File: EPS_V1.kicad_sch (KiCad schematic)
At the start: 0 parts

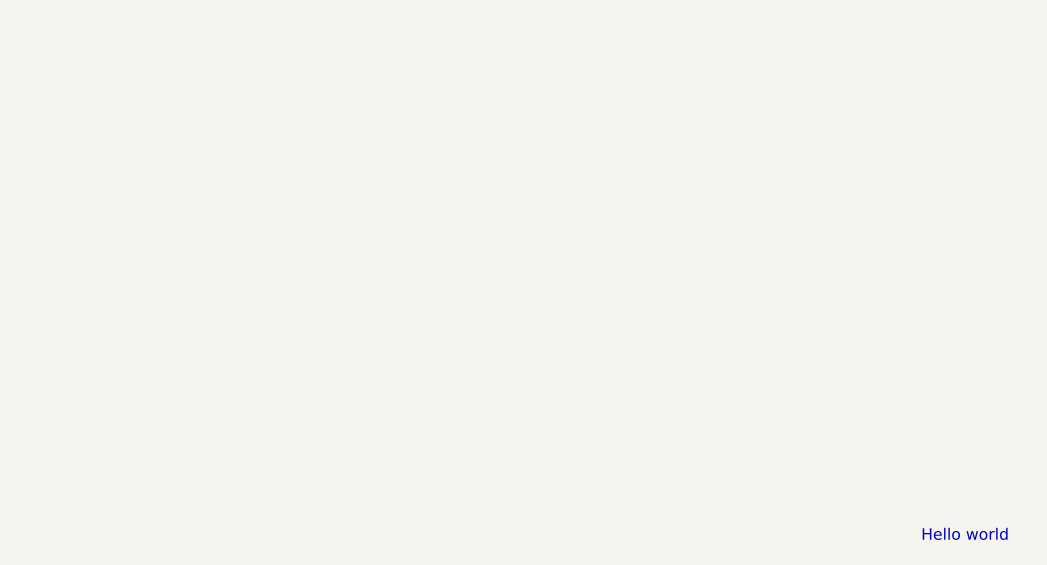
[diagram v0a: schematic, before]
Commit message: Add connectors, 5V & 3V3 buck converters, 1 battery pack & charger
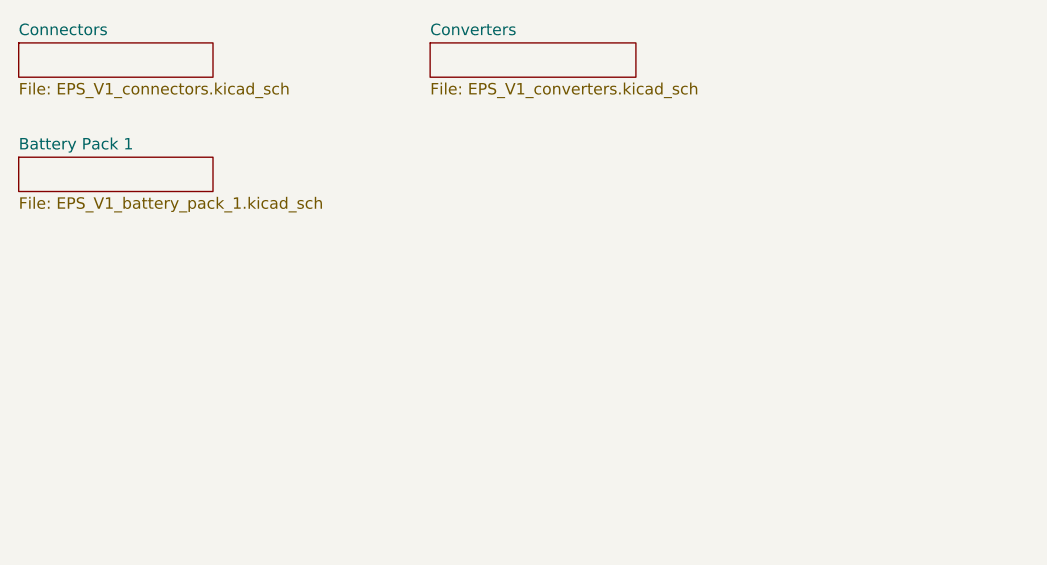
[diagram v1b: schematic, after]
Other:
- added sheet Battery Pack 1 (EPS_V1_battery_pack_1.kicad_sch)
- added sheet Connectors (EPS_V1_connectors.kicad_sch)
- added sheet Converters (EPS_V1_converters.kicad_sch)
- note removed: "Hello world"
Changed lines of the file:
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@@
 	(generator_version "9.0")
 	(paper "A4")
-	(text "Hello world"
+	(sheet
+		(at 80.01 31.75)
+		(size 22.86 3.81)
 		(exclude_from_sim no)
-		(at 139.446 86.614 0)
-		(effects
-			(font
-				(size 1.27 1.27)
+		(in_bom yes)
+		(on_board yes)
+		(dnp no)
+		(fields_autoplaced yes)
+		(stroke
+			(width 0.1524)
+			(type solid)
+		)
+		(fill
+			(color 0 0 0 0.0000)
+		)
+		(property "Sheetname" "Converters"
+			(at 80.01 31.0384 0)
+			(effects
+				(font
+					(size 1.27 1.27)
+				)
+				(justify left bottom)
 			)
 		)
+		(property "Sheetfile" "EPS_V1_converters.kicad_sch"
+			(at 80.01 36.1446 0)
+			(effects
+				(font
+					(size 1.27 1.27)
+				)
+				(justify left top)
+			)
+		)
+		(instances
+			(project "EPS_V1"
+				(path "/85157432-5d03-48fa-ab40-27ed3d133f47"
+					(page "3")
+				)
+			)
+		)
+	)
+	(sheet
+		(at 34.29 44.45)
+		(size 21.59 3.81)
+		(exclude_from_sim no)
+		(in_bom yes)
+		(on_board yes)
+		(dnp no)
+		(fields_autoplaced yes)
+		(stroke
+			(width 0.1524)
+			(type solid)
+		)
+		(fill
+			(color 0 0 0 0.0000)
+		)
+		(property "Sheetname" "Battery Pack 1"
+			(at 34.29 43.7384 0)
+			(effects
+				(font
+					(size 1.27 1.27)
+				)
+				(justify left bottom)
+			)
+		)
+		(property "Sheetfile" "EPS_V1_battery_pack_1.kicad_sch"
+			(at 34.29 48.8446 0)
+			(effects
+				(font
+					(size 1.27 1.27)
+				)
+				(justify left top)
+			)
+		)
+		(instances
+			(project "EPS_V1"
+				(path "/85157432-5d03-48fa-ab40-27ed3d133f47"
+					(page "4")
+				)
+			)
+		)
+	)
+	(sheet
+		(at 34.29 31.75)
+		(size 21.59 3.81)
+		(exclude_from_sim no)
+		(in_bom yes)
+		(on_board yes)
+		(dnp no)
+		(fields_autoplaced yes)
+		(stroke
+			(width 0.1524)
+			(type solid)
+		)
+		(fill
+			(color 0 0 0 0.0000)
+		)
+		(property "Sheetname" "Connectors"
+			(at 34.29 31.0384 0)
+			(effects
+				(font
+					(size 1.27 1.27)
+				)
+				(justify left bottom)
+			)
+		)
+		(property "Sheetfile" "EPS_V1_connectors.kicad_sch"
+			(at 34.29 36.1446 0)
+			(effects
+				(font
+					(size 1.27 1.27)
+				)
+				(justify left top)
+			)
+		)
+		(instances
+			(project "EPS_V1"
+				(path "/85157432-5d03-48fa-ab40-27ed3d133f47"
+					(page "2")
+				)
+			)
+		)

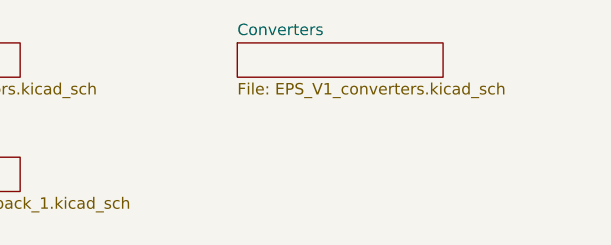
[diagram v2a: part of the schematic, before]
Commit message: Add power switching IC
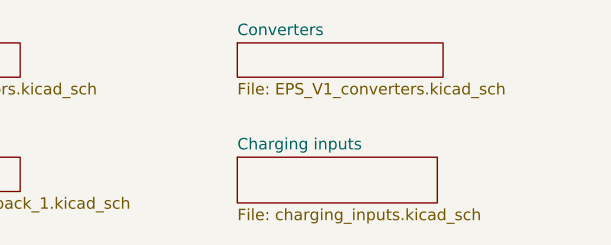
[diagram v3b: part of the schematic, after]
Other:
- added sheet Charging inputs (charging_inputs.kicad_sch)
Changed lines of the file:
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@@
 	(paper "A4")
+	(sheet
+		(at 80.01 44.45)
+		(size 22.225 5.08)
+		(exclude_from_sim no)
+		(in_bom yes)
+		(on_board yes)
+		(dnp no)
+		(fields_autoplaced yes)
+		(stroke
+			(width 0.1524)
+			(type solid)
+		)
+		(fill
+			(color 0 0 0 0)
+		)
+		(property "Sheetname" "Charging inputs"
+			(at 80.01 43.7384 0)
+			(show_name no)
+			(do_not_autoplace no)
+			(effects
+				(font
+					(size 1.27 1.27)
+				)
+				(justify left bottom)
+			)
+		)
+		(property "Sheetfile" "charging_inputs.kicad_sch"
+			(at 80.01 50.1146 0)
+			(show_name no)
+			(do_not_autoplace no)
+			(effects
+				(font
+					(size 1.27 1.27)
+				)
+				(justify left top)
+			)
+		)
+		(instances
+			(project "EPS_V1"
+				(path "/85157432-5d03-48fa-ab40-27ed3d133f47"
+					(page "1")
+				)
+			)
+		)
+	)
 	(sheet
 		(at 80.01 31.75)

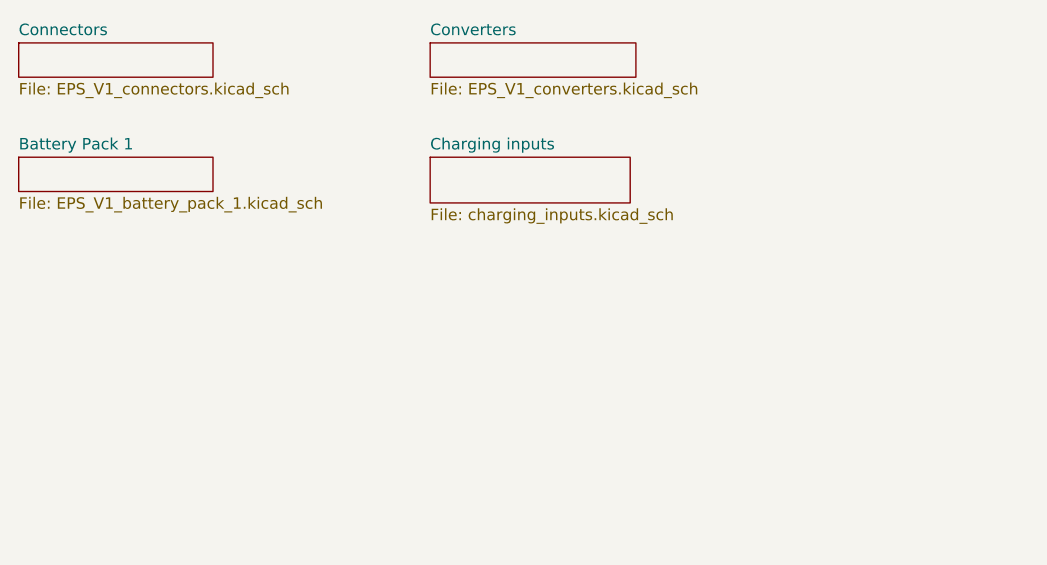
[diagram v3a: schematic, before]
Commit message: Add other battery packs, connect all ALRT signals, assign footprints for new components, make inhibit switch footprints
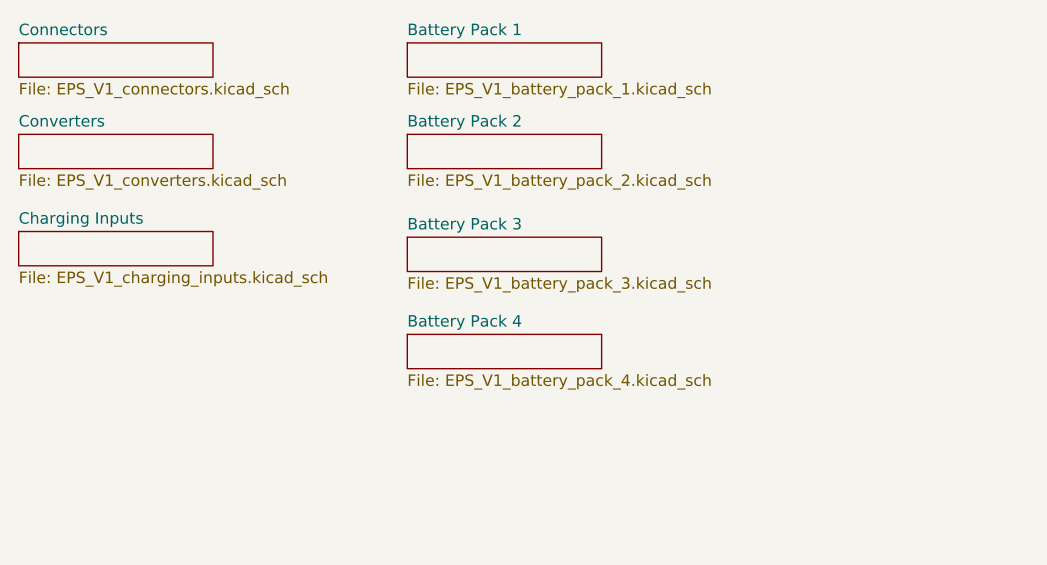
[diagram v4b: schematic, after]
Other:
- sheet Charging inputs renamed Charging Inputs
- added sheet Battery Pack 2 (EPS_V1_battery_pack_2.kicad_sch)
- added sheet Battery Pack 3 (EPS_V1_battery_pack_3.kicad_sch)
- added sheet Battery Pack 4 (EPS_V1_battery_pack_4.kicad_sch)
- sheet Charging Inputs: file charging_inputs.kicad_sch -> EPS_V1_charging_inputs.kicad_sch
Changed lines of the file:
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@@
 	(paper "A4")
 	(sheet
-		(at 80.01 44.45)
-		(size 22.225 5.08)
-		(exclude_from_sim no)
-		(in_bom yes)
-		(on_board yes)
-		(dnp no)
-		(fields_autoplaced yes)
-		(stroke
-			(width 0.1524)
-			(type solid)
-		)
-		(fill
-			(color 0 0 0 0)
-		)
-		(property "Sheetname" "Charging inputs"
-			(at 80.01 43.7384 0)
-			(show_name no)
-			(do_not_autoplace no)
-			(effects
-				(font
-					(size 1.27 1.27)
-				)
-				(justify left bottom)
-			)
-		)
-		(property "Sheetfile" "charging_inputs.kicad_sch"
-			(at 80.01 50.1146 0)
+		(at 77.47 41.91)
+		(size 21.59 3.81)
+		(exclude_from_sim no)
+		(in_bom yes)
+		(on_board yes)
+		(dnp no)
+		(fields_autoplaced yes)
+		(stroke
+			(width 0.1524)
+			(type solid)
+		)
+		(fill
+			(color 0 0 0 0)
+		)
+		(property "Sheetname" "Battery Pack 2"
+			(at 77.47 41.1984 0)
+			(show_name no)
+			(do_not_autoplace no)
+			(effects
+				(font
+					(size 1.27 1.27)
+				)
+				(justify left bottom)
+			)
+		)
+		(property "Sheetfile" "EPS_V1_battery_pack_2.kicad_sch"
+			(at 77.47 46.3046 0)
+			(show_name no)
+			(do_not_autoplace no)
+			(effects
+				(font
+					(size 1.27 1.27)
+				)
+				(justify left top)
+			)
+		)
+		(instances
+			(project "EPS_V1"
+				(path "/85157432-5d03-48fa-ab40-27ed3d133f47"
+					(page "5")
+				)
+			)
+		)
+	)
+	(sheet
+		(at 34.29 52.705)
+		(size 21.59 3.81)
+		(exclude_from_sim no)
+		(in_bom yes)
+		(on_board yes)
+		(dnp no)
+		(fields_autoplaced yes)
+		(stroke
+			(width 0.1524)
+			(type solid)
+		)
+		(fill
+			(color 0 0 0 0)
+		)
+		(property "Sheetname" "Charging Inputs"
+			(at 34.29 51.9934 0)
+			(show_name no)
+			(do_not_autoplace no)
+			(effects
+				(font
+					(size 1.27 1.27)
+				)
+				(justify left bottom)
+			)
+		)
+		(property "Sheetfile" "EPS_V1_charging_inputs.kicad_sch"
+			(at 34.29 57.0996 0)
 			(show_name no)
 			(do_not_autoplace no)
@@
 	)
 	(sheet
-		(at 80.01 31.75)
-		(size 22.86 3.81)
+		(at 77.47 64.135)
+		(size 21.59 3.81)
+		(exclude_from_sim no)
+		(in_bom yes)
+		(on_board yes)
+		(dnp no)
+		(fields_autoplaced yes)
+		(stroke
+			(width 0.1524)
+			(type solid)
+		)
+		(fill
+			(color 0 0 0 0)
+		)
+		(property "Sheetname" "Battery Pack 4"
+			(at 77.47 63.4234 0)
+			(show_name no)
+			(do_not_autoplace no)
+			(effects
+				(font
+					(size 1.27 1.27)
+				)
+				(justify left bottom)
+			)
+		)
+		(property "Sheetfile" "EPS_V1_battery_pack_4.kicad_sch"
+			(at 77.47 68.5296 0)
+			(show_name no)
+			(do_not_autoplace no)
+			(effects
+				(font
+					(size 1.27 1.27)
+				)
+				(justify left top)
+			)
+		)
+		(instances
+			(project "EPS_V1"
+				(path "/85157432-5d03-48fa-ab40-27ed3d133f47"
+					(page "7")
+				)
+			)
+		)
+	)
+	(sheet
+		(at 34.29 41.91)
+		(size 21.59 3.81)
 		(exclude_from_sim no)
 		(in_bom yes)
@@
 		)
 		(property "Sheetname" "Converters"
-			(at 80.01 31.0384 0)
+			(at 34.29 41.1984 0)
 			(show_name no)
 			(do_not_autoplace no)
@@
 		)
 		(property "Sheetfile" "EPS_V1_converters.kicad_sch"
-			(at 80.01 36.1446 0)
+			(at 34.29 46.3046 0)
 			(show_name no)
 			(do_not_autoplace no)
@@
 	)
 	(sheet
-		(at 34.29 44.45)
+		(at 77.47 31.75)
 		(size 21.59 3.81)
 		(exclude_from_sim no)
@@
 		)
 		(property "Sheetname" "Battery Pack 1"
-			(at 34.29 43.7384 0)
+			(at 77.47 31.0384 0)
 			(show_name no)
 			(do_not_autoplace no)
@@
 		)
 		(property "Sheetfile" "EPS_V1_battery_pack_1.kicad_sch"
-			(at 34.29 48.8446 0)
+			(at 77.47 36.1446 0)
 			(show_name no)
 			(do_not_autoplace no)
@@
 				)
 			)
+		)
+	)
+	(sheet
+		(at 77.47 53.34)
+		(size 21.59 3.81)
+		(exclude_from_sim no)
+		(in_bom yes)
+		(on_board yes)
+		(dnp no)
+		(fields_autoplaced yes)
+		(stroke
+			(width 0.1524)
+			(type solid)
+		)
+		(fill
+			(color 0 0 0 0)
+		)
+		(property "Sheetname" "Battery Pack 3"
+			(at 77.47 52.6284 0)
+			(show_name no)
+			(do_not_autoplace no)
+			(effects
+				(font
+					(size 1.27 1.27)
+				)
+				(justify left bottom)
+			)
+		)
+		(property "Sheetfile" "EPS_V1_battery_pack_3.kicad_sch"
+			(at 77.47 57.7346 0)
+			(show_name no)
+			(do_not_autoplace no)
+			(effects
+				(font
+					(size 1.27 1.27)
+				)
+				(justify left top)
+			)
+		)
+		(instances
+			(project "EPS_V1"
+				(path "/85157432-5d03-48fa-ab40-27ed3d133f47"
+					(page "6")
+				)
+			)
